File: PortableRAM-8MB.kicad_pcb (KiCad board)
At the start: 4 copper layers, 123 x 81 mm, 37 parts, among them J1 RAM Connector, J2 JTAG_Header_2.54mm_1x06, U1 ATF1502ASL, U11 74HC245, U12 74HC245, U2 AS6C8008-55TIN, U3 AS6C8008-55TIN, U4 AS6C8008-55TIN, U5 AS6C8008-55TIN, U6 AS6C8008-55TIN, U7 AS6C8008-55TIN, U8 AS6C8008-55TIN, U9 AS6C8008-55TIN

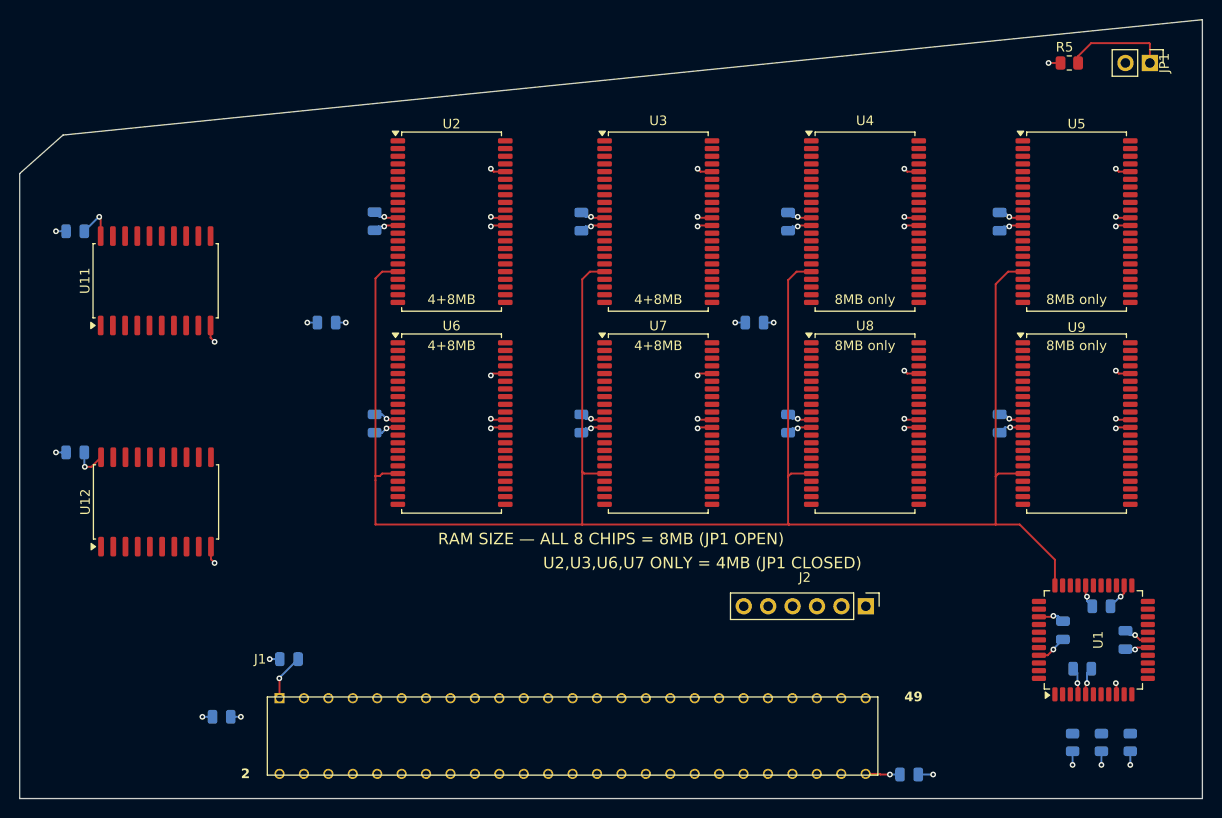
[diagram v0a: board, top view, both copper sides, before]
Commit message: PCB: FreeRouting complete — fully routed, DRC clean
Imported autorouted .ses (buses on F.Cu/B.Cu; inner layers stay pure
GND/+5V planes). 3507 segments, 439 vias. DRC: 0 errors, 0 unconnected
pads, 0 duplicate copper. All 220 locked power+BANKSEL segments and 69
vias survived import unchanged. FreeRouting's ~30 "unrouted" were
plane connections it can't see; resolved on zone refill (the v0.2
lesson). Remaining 5 items all cosmetic silk/footprint-filter.

Co-Authored-By: Claude Fable 5 <noreply@anthropic.com>
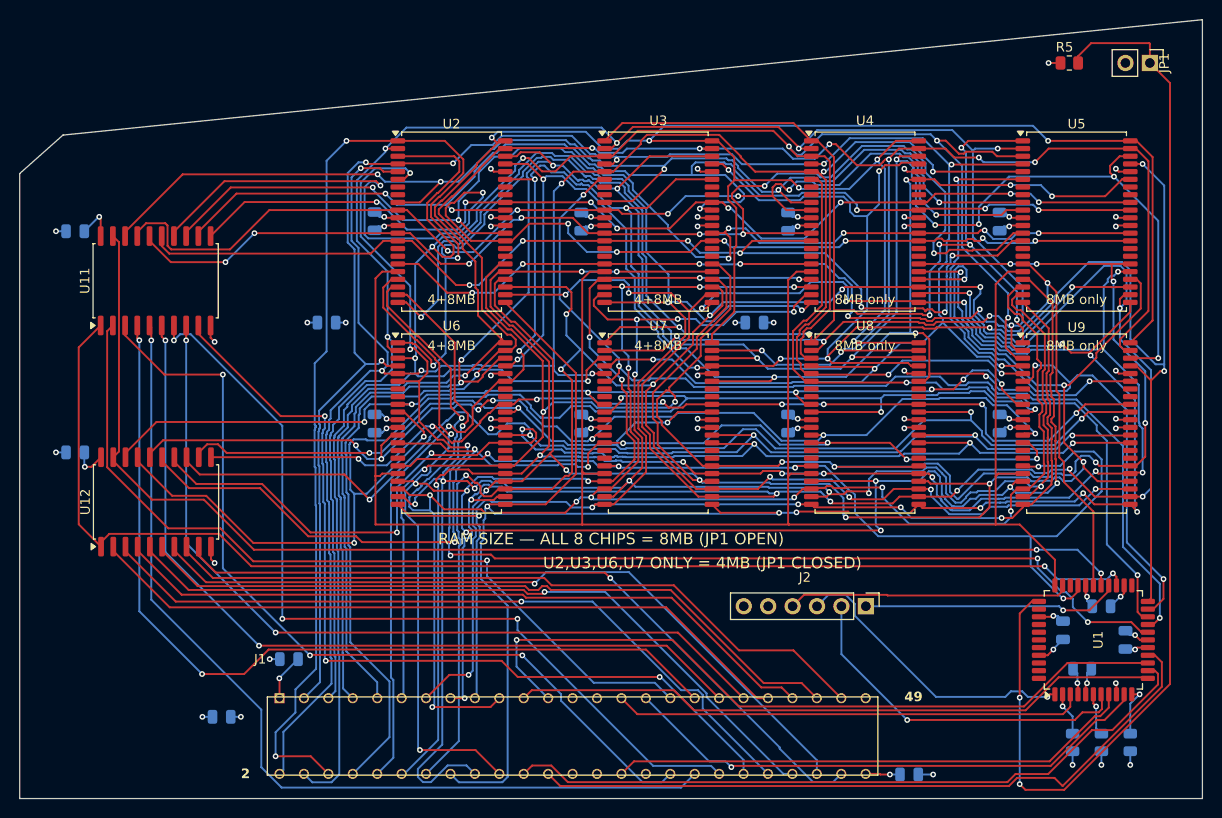
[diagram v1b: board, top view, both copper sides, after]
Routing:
- net /A5: track 0.00 -> 281.4 mm, vias 0 -> 11
- net /A6: track 0.00 -> 250.2 mm, vias 0 -> 7
- net /A19: track 0.00 -> 244.2 mm, vias 0 -> 14
- net /A3: track 0.00 -> 238.4 mm, vias 0 -> 7
- net /A8: track 0.00 -> 236.7 mm, vias 0 -> 11
- net /A7: track 0.00 -> 228.8 mm, vias 0 -> 9
- net /OE: track 0.00 -> 224.7 mm, vias 0 -> 10
- net /A1: track 0.00 -> 220.2 mm, vias 0 -> 9
- net /A9: track 0.00 -> 219.7 mm, vias 0 -> 11
- net /A15: track 0.00 -> 219.3 mm, vias 0 -> 11
- net /A14: track 0.00 -> 215.7 mm, vias 0 -> 11
- net /A17: track 0.00 -> 215.6 mm, vias 0 -> 12
- net /A16: track 0.00 -> 215.5 mm, vias 0 -> 8
- net /A2: track 0.00 -> 213.7 mm, vias 0 -> 9
- net /A12: track 0.00 -> 213.5 mm, vias 0 -> 9
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
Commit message: PCB: silk nudges + plot v2 fab package
C14 and JP1 reference labels nudged clear of overlaps (silk_overlap
and one silk_over_copper resolved). DRC now matches v0.2 accepted
baseline: 0 unconnected, only inherent J1 silk/lib items + cosmetic
footprint-filter notes. Plotted 11 Gerbers + PTH/NPTH drills, zipped.

Co-Authored-By: Claude Fable 5 <noreply@anthropic.com>
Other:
- board text added: "1"
- board text removed: "2"

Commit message: v2 PCB: add TP1 ground test point on left edge for bench clip
Left edge @ (71,125), clear of parts (11mm to nearest). 2.8mm pad /
1.2mm plated hole on GND net -- alligator-clip target for bench
ground / scope reference. Ground-only by choice (a 5V edge pad risks
shorting; feed +5V via J2 pin 5 instead).

Connects to In1 GND plane; 0 unconnected. The 2 clearance DRC items
are stale-fill artifacts (In2 +5V plane needs to carve clearance
around the new GND hole) -- clear on zone refill (B) in KiCad, done
at the next re-plot before ordering.

Co-Authored-By: Claude Fable 5 <noreply@anthropic.com>
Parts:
- added TP1: GND, TestPoint_GND, F.Cu at (71.0, 125.0)
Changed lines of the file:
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@@
 	(net 154 "unconnected-(U9-NC-Pad30)")
 	(net 155 "unconnected-(U9-NC-Pad16)")
+	(footprint "TestPoint_GND"
+		(layer "F.Cu")
+		(at 71 125)
+		(property "Reference" "TP1"
+			(at 0 -3 0)
+			(layer "F.SilkS")
+			(effects (font (size 1 1) (thickness 0.15)))
+		)
+		(property "Value" "GND"
+			(at 0 3.2 0)
+			(layer "F.SilkS")
+			(effects (font (size 1.2 1.2) (thickness 0.2)))
+		)
+		(attr through_hole)
+		(fp_circle
+			(center 0 0) (end 1.75 0)
+			(stroke (width 0.15) (type solid)) (fill none)
+			(layer "F.SilkS")
+		)
+		(pad "1" thru_hole circle
+			(at 0 0) (size 2.8 2.8) (drill 1.2)
+			(layers "*.Cu" "*.Mask")
+			(net 1 "GND")
+		)
+	)
 	(footprint "Package_SO:TSOP-II-44_10.16x18.41mm_P0.8mm"
 		(layer "F.Cu")
